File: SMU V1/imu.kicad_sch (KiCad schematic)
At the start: 0 parts

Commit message: i forget what i changed
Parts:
- added C601, C602: 100n, Capacitor_SMD:C_0402_1005Metric_Pad0.74x0.62mm_HandSolder, symbol bfr_capacitors:CL05B104KO5NNNC
- added U601: LSM6DSOTR, Package_LGA:LGA-14_3x2.5mm_P0.5mm_LayoutBorder3x4y, symbol bfr_utilities:LSM6DSO
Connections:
- new net GND: C601.2, C602.2, U601.2 (SDx), U601.3 (SCx), U601.6 (GND), U601.7 (GND )
- new net IMU_INT1: U601.4 (INT1)
- new net IMU_INT2: U601.9 (INT2)
- new net IMU_SPI.CS: U601.12 (CS)
- new net IMU_SPI.MISO: U601.1 (I2C_SA0)
- new net IMU_SPI.MOSI: U601.14 (I2C_SDA)
- new net IMU_SPI.SCK: U601.13 (I2C_SCL)
- new net PP3300_IMU_VDD: C601.1, C602.1, U601.5 (VDDIO), U601.8 (VDD)
- no-connect marks 0 -> 2
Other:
- added sheet GPS Power (low_noise_ldo.kicad_sch)

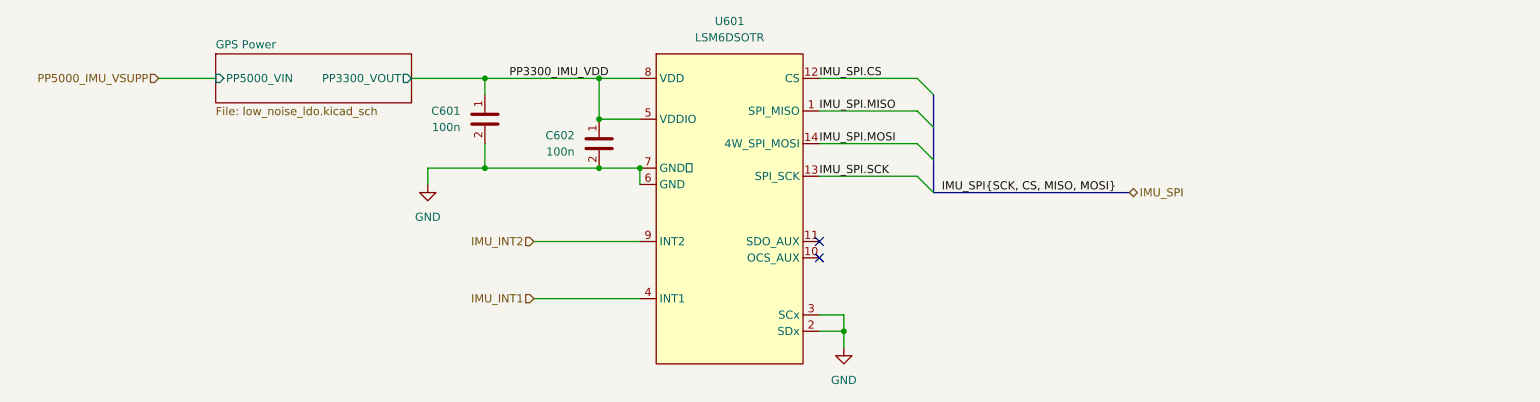
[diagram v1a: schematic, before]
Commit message: halfway done with routing, still needs antenna
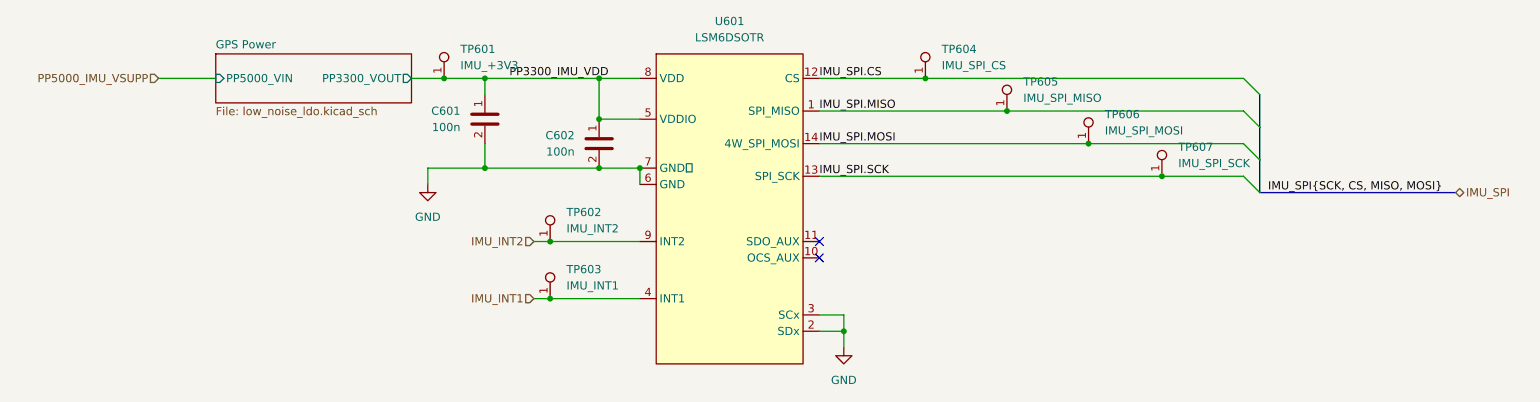
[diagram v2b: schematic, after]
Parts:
- added TP601: IMU_+3V3, bfr_utilities:TestPoint_Keystone_5019_Miniature, symbol bfr_utilities:SMD_Test_Point
- added TP602: IMU_INT2, bfr_utilities:TestPoint_Keystone_5019_Miniature, symbol bfr_utilities:SMD_Test_Point
- added TP603: IMU_INT1, bfr_utilities:TestPoint_Keystone_5019_Miniature, symbol bfr_utilities:SMD_Test_Point
- added TP604: IMU_SPI_CS, bfr_utilities:TestPoint_Keystone_5019_Miniature, symbol bfr_utilities:SMD_Test_Point
- added TP605: IMU_SPI_MISO, bfr_utilities:TestPoint_Keystone_5019_Miniature, symbol bfr_utilities:SMD_Test_Point
- added TP606: IMU_SPI_MOSI, bfr_utilities:TestPoint_Keystone_5019_Miniature, symbol bfr_utilities:SMD_Test_Point
- added TP607: IMU_SPI_SCK, bfr_utilities:TestPoint_Keystone_5019_Miniature, symbol bfr_utilities:SMD_Test_Point
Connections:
- net IMU_INT1: now also TP603.1
- net IMU_INT2: now also TP602.1
- net IMU_SPI.CS: now also TP604.1
- net IMU_SPI.MISO: now also TP605.1
- net IMU_SPI.MOSI: now also TP606.1
- net IMU_SPI.SCK: now also TP607.1
- net PP3300_IMU_VDD: now also TP601.1
